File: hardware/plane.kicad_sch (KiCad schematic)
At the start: 51 parts, among them J1 USB_B_Micro, J10 Conn_01x05_Pin, J11 Conn_01x04_Pin, J2 Conn_Coaxial, J3 Conn_01x03, J4 Conn_01x03, J5 Conn_01x03, J6 Conn_01x03, J7 Conn_01x02, J8 Conn_01x03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

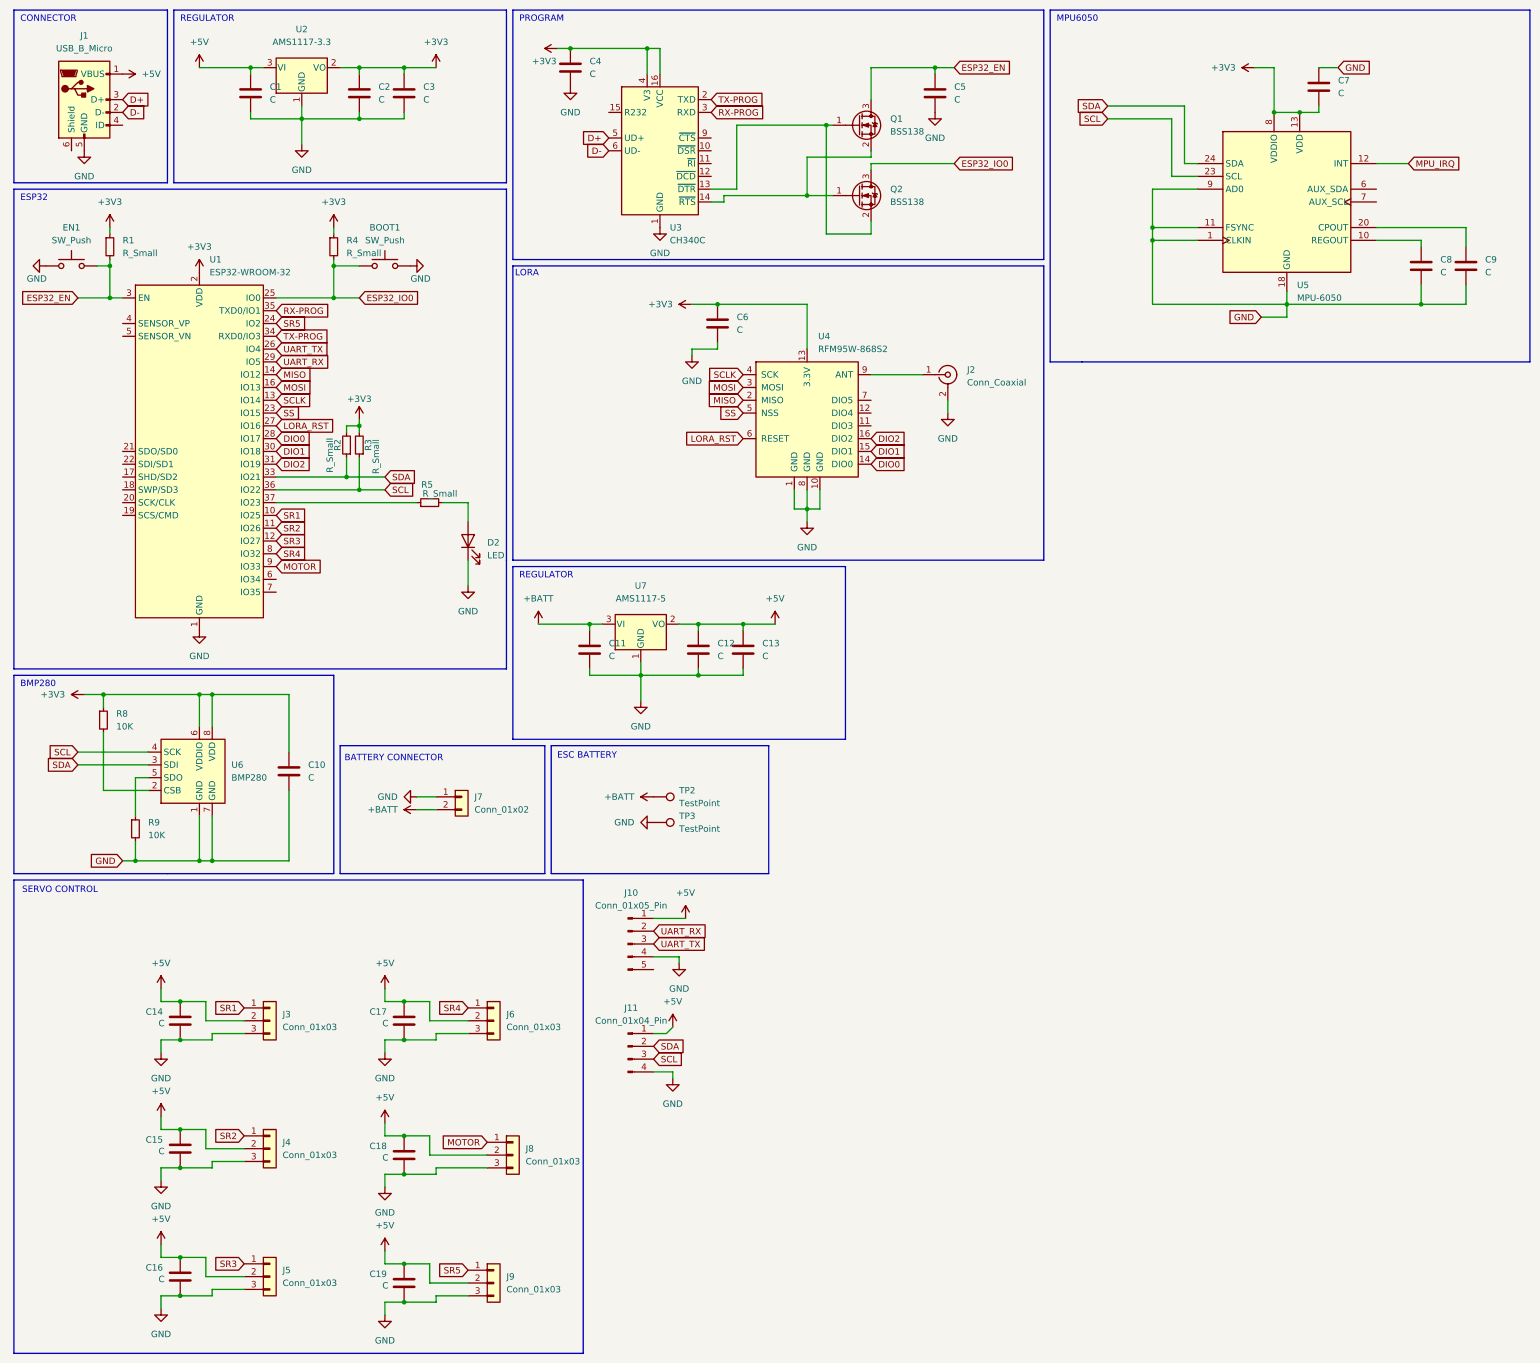
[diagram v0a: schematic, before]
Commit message: add nrf24l01 connector
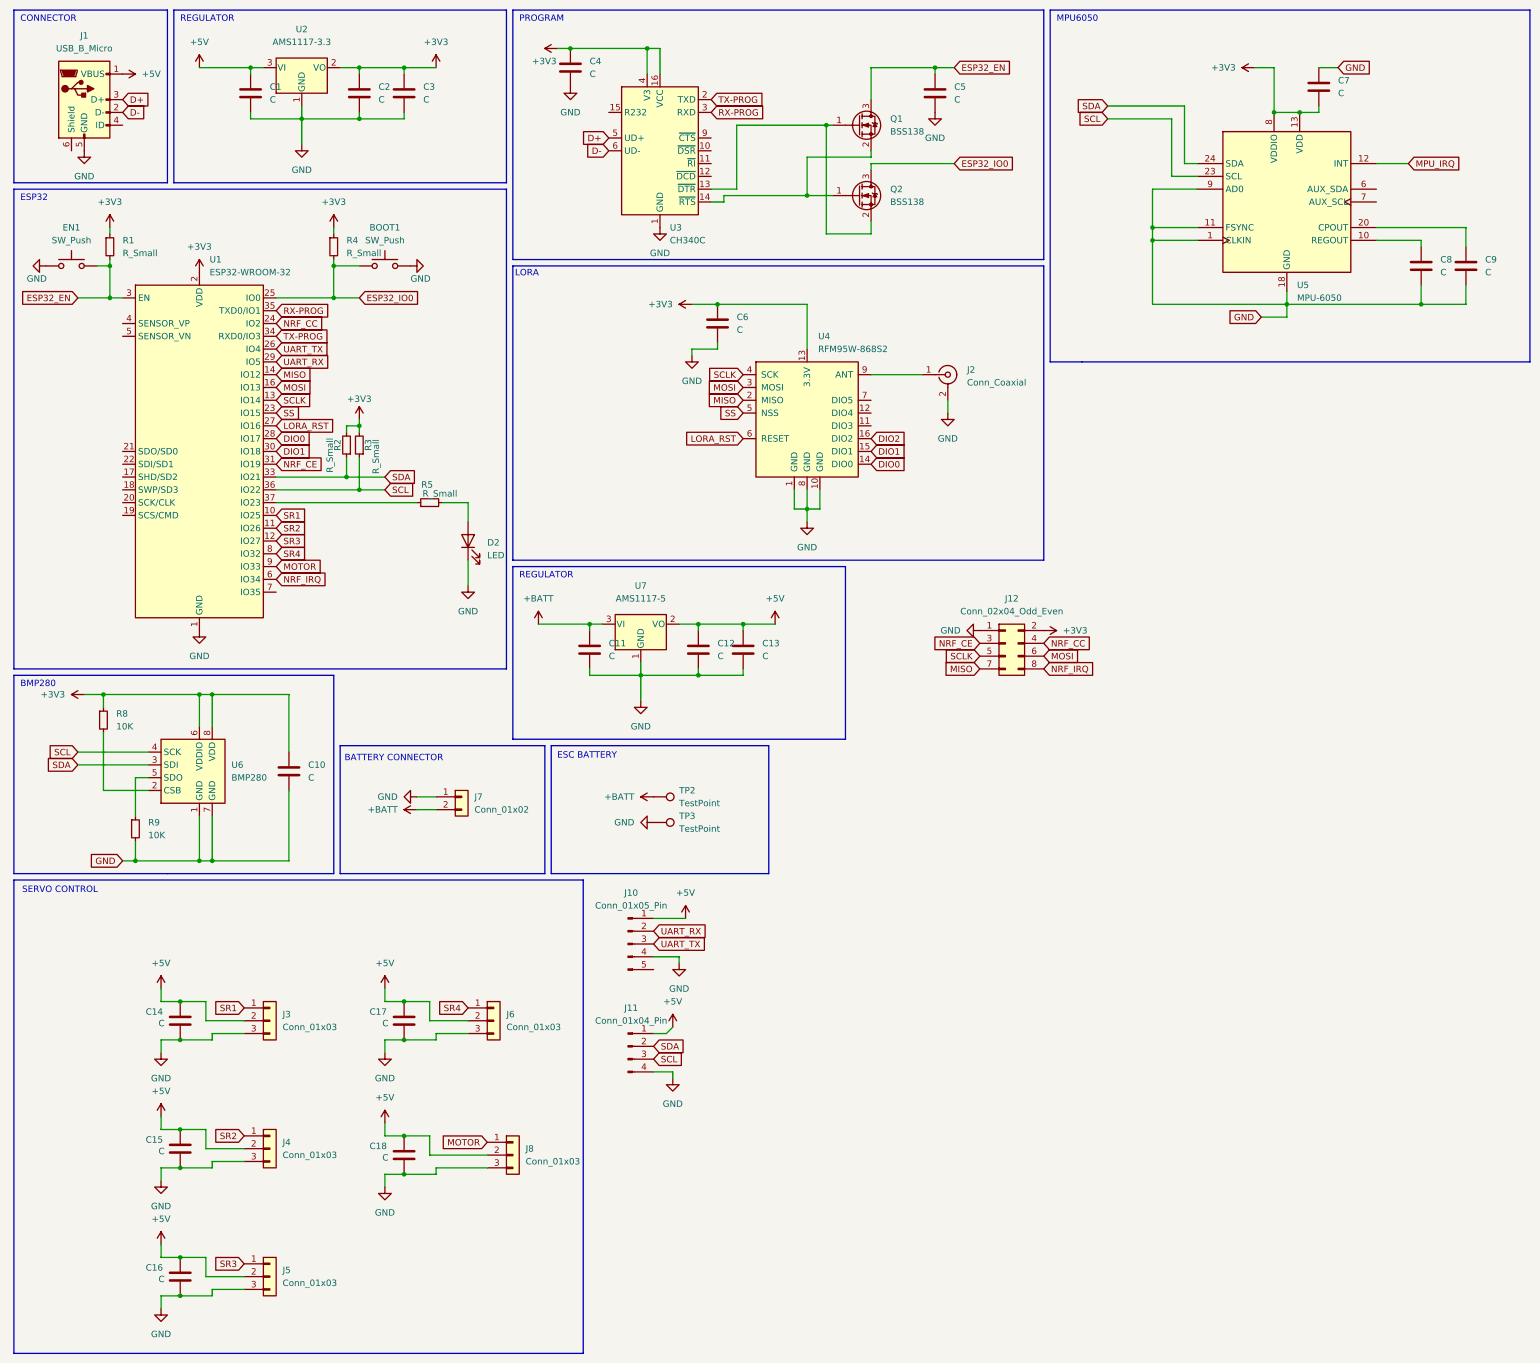
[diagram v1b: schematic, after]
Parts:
- removed C19: C, Capacitor_SMD:C_0603_1608Metric, symbol Device:C
- removed J9: Conn_01x03, Connector_PinHeader_2.54mm:PinHeader_1x03_P2.54mm_Vertical, symbol Connector_Generic:Conn_01x03
- added J12: Conn_02x04_Odd_Even, Connector_PinHeader_2.54mm:PinHeader_2x04_P2.54mm_Vertical, symbol Connector_Generic:Conn_02x04_Odd_Even
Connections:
- net +3V3: now also J12.2 (Pin_2)
- net DIO2: no longer U1.31 (IO19)
- net GND: now also J12.1 (Pin_1)
- net MISO: now also J12.7 (Pin_7)
- net MOSI: now also J12.6 (Pin_6)
- net SCLK: now also J12.5 (Pin_5)
- net NRF_IRQ: now reaches U1.6 (IO34)
- net NRF_IRQ: now also J12.8 (Pin_8)
- net SR5 renamed NRF_CC
- net NRF_CC: now also J12.4 (Pin_4)
- new net NRF_CE: J12.3 (Pin_3), U1.31 (IO19)
